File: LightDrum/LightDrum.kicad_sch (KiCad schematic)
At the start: 9 parts, among them U1 STR485

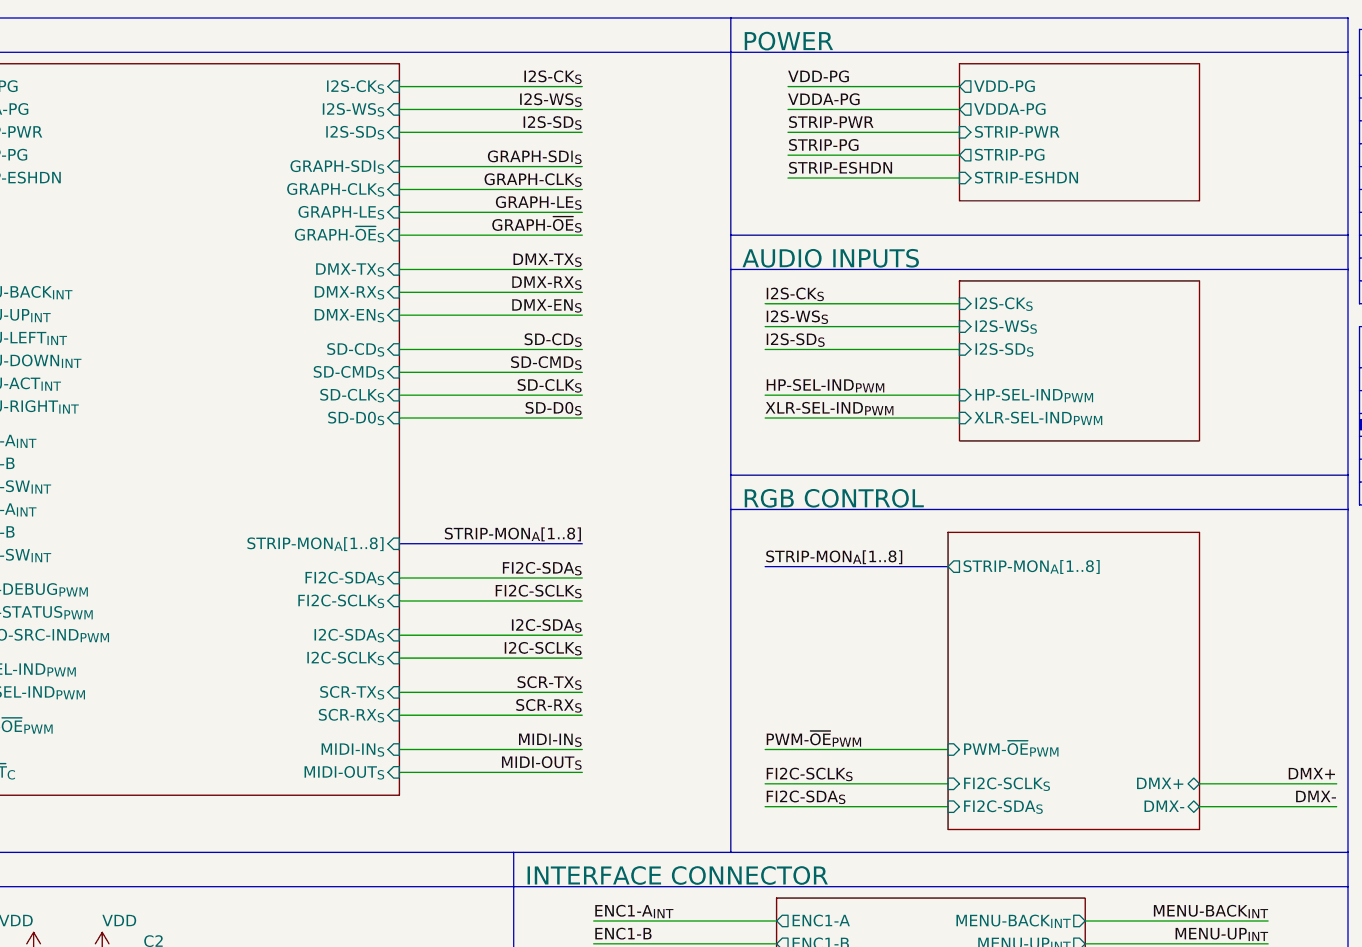
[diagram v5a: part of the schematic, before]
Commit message: Replace DSub with much better ECU conn
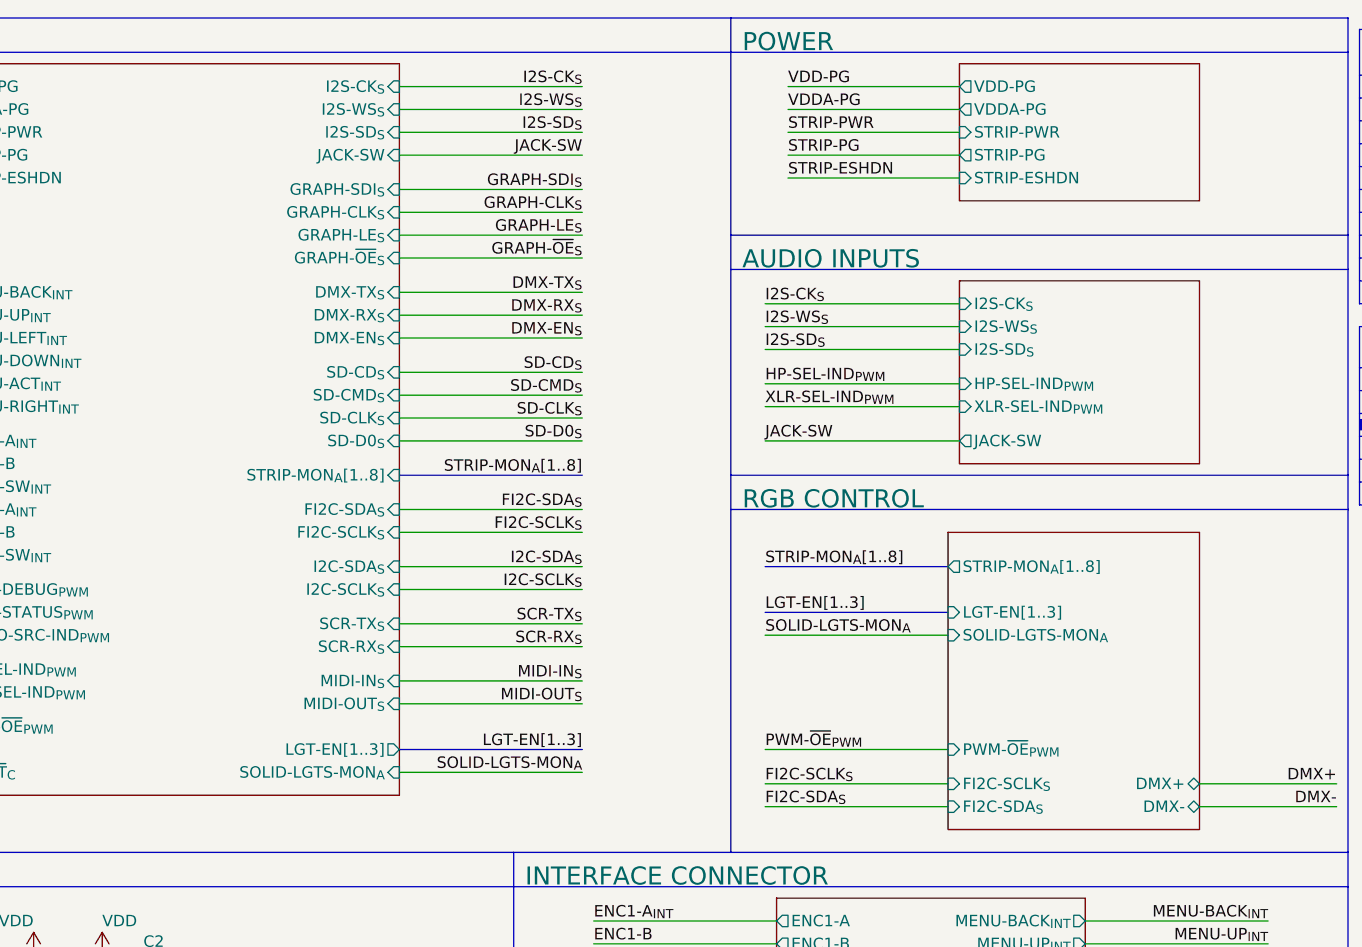
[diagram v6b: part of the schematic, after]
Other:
- sheet AUDIO INPUTS ports: added JACK-SW; removed none
- sheet MICROCONTROLLER ports: added JACK-SW, LGT-EN[1..3], SOLID-LGTS-MON_{A}; removed none
- sheet RGB CONTROL ports: added LGT-EN[1..3], SOLID-LGTS-MON_{A}; removed none

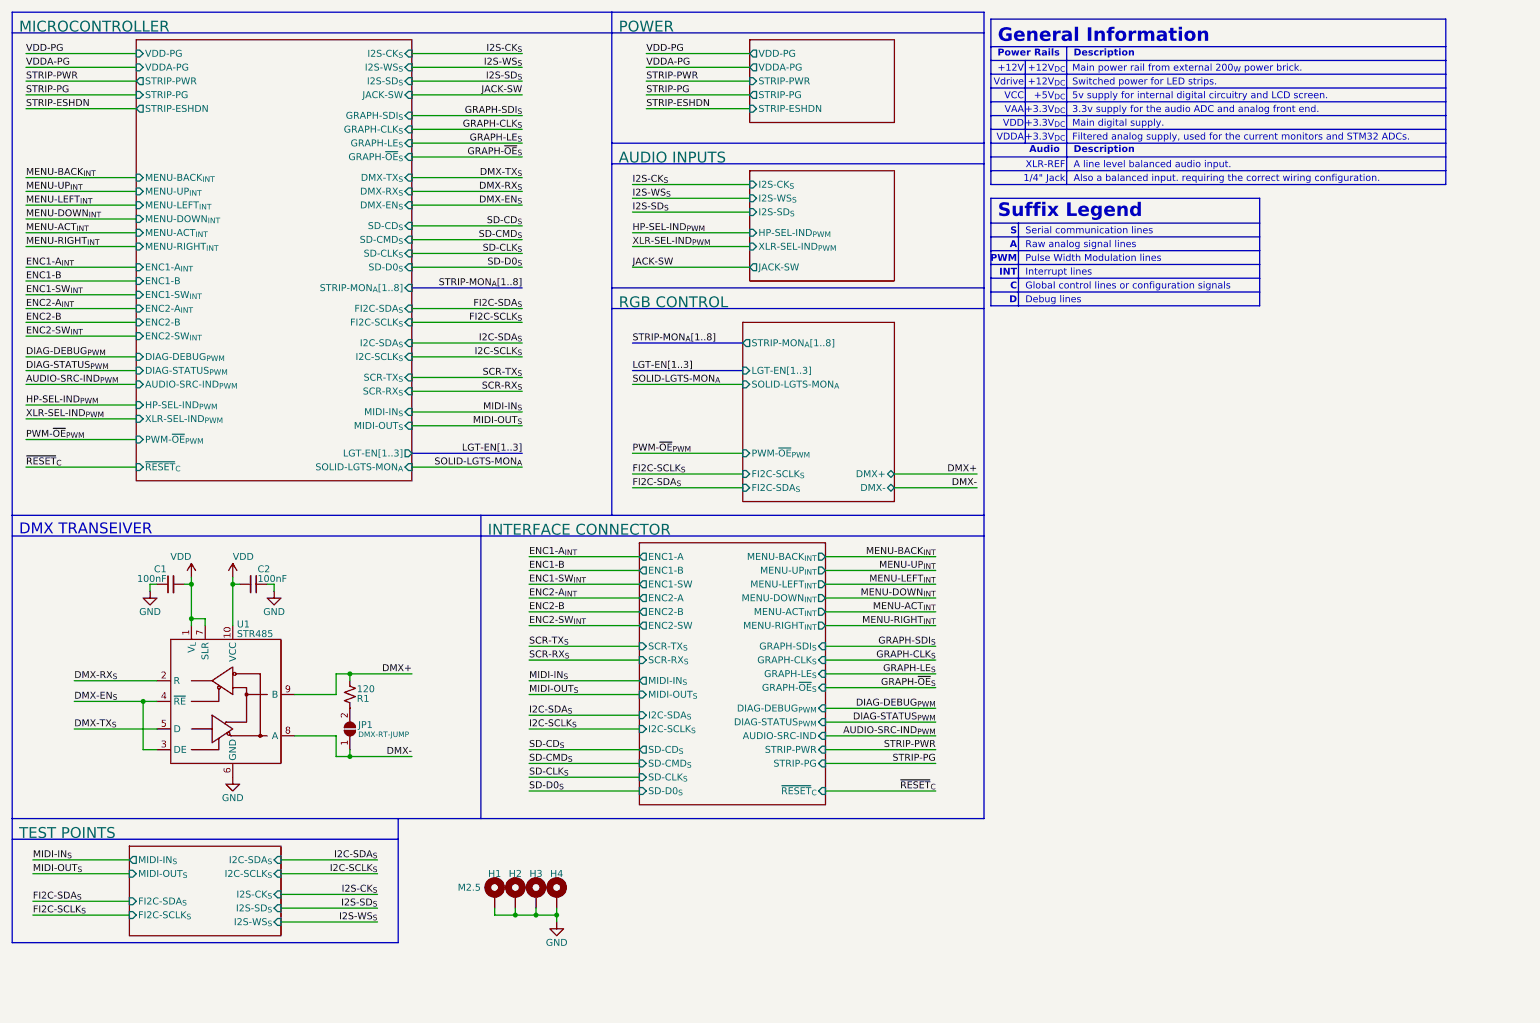
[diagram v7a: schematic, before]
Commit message: Fix schematic layout
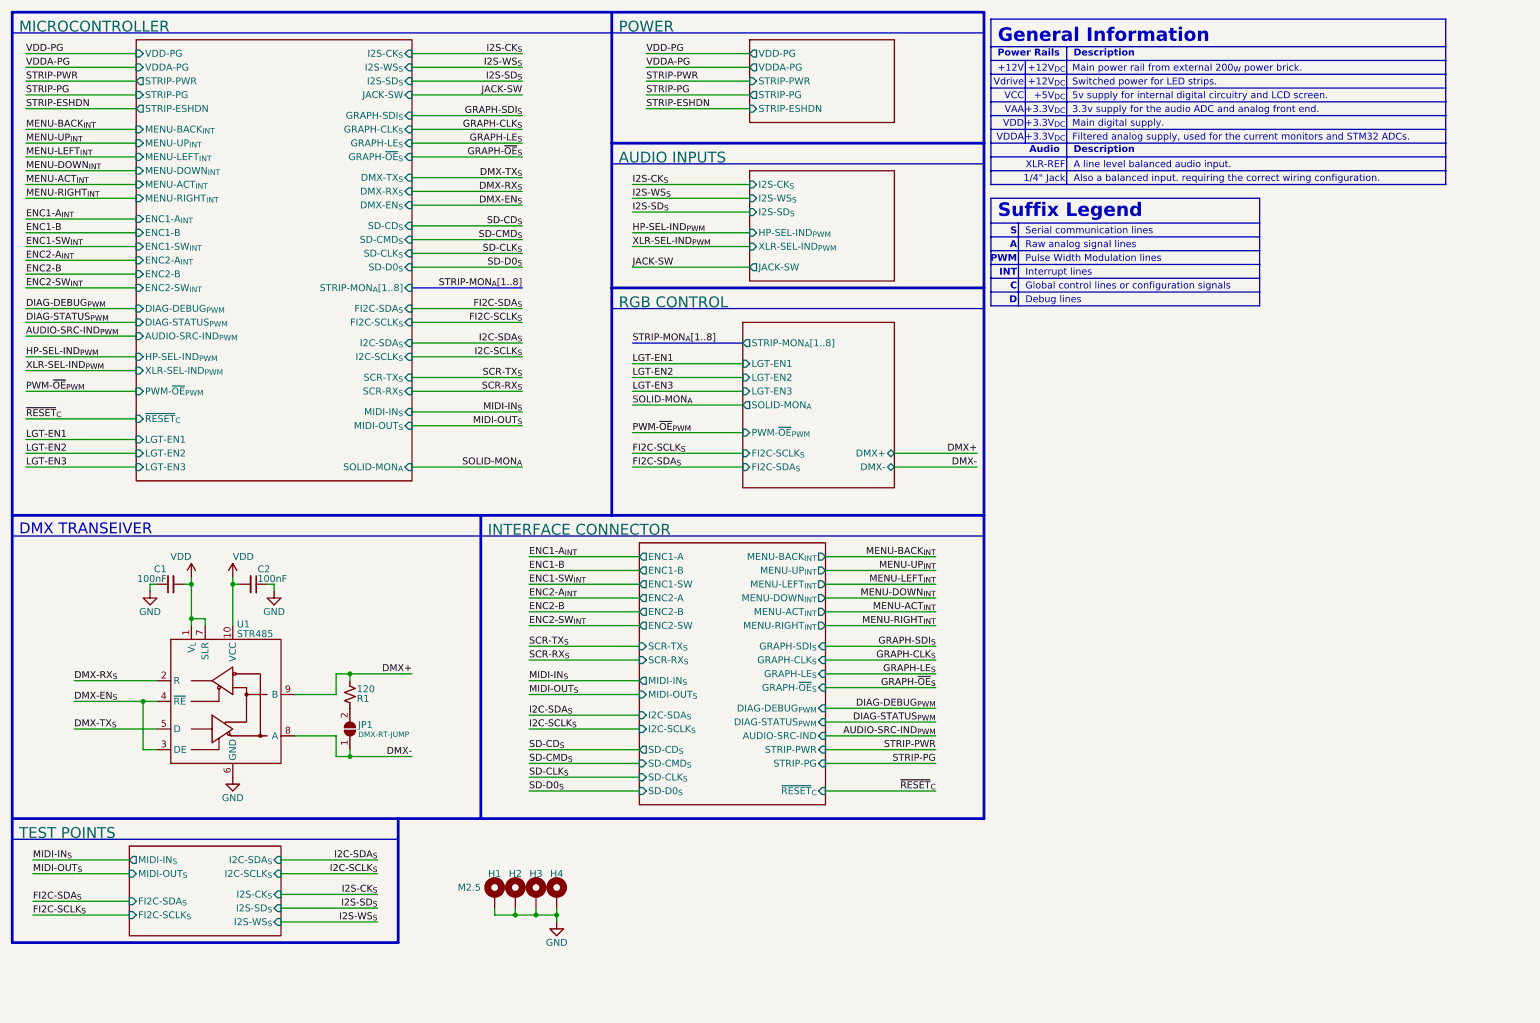
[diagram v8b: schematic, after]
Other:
- sheet MICROCONTROLLER ports: added LGT-EN1, LGT-EN2, LGT-EN3, SOLID-MON_{A}; removed LGT-EN[1..3], SOLID-LGTS-MON_{A}
- sheet RGB CONTROL ports: added LGT-EN1, LGT-EN2, LGT-EN3, SOLID-MON_{A}; removed LGT-EN[1..3], SOLID-LGTS-MON_{A}
